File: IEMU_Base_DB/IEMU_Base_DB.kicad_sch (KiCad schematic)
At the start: 0 parts

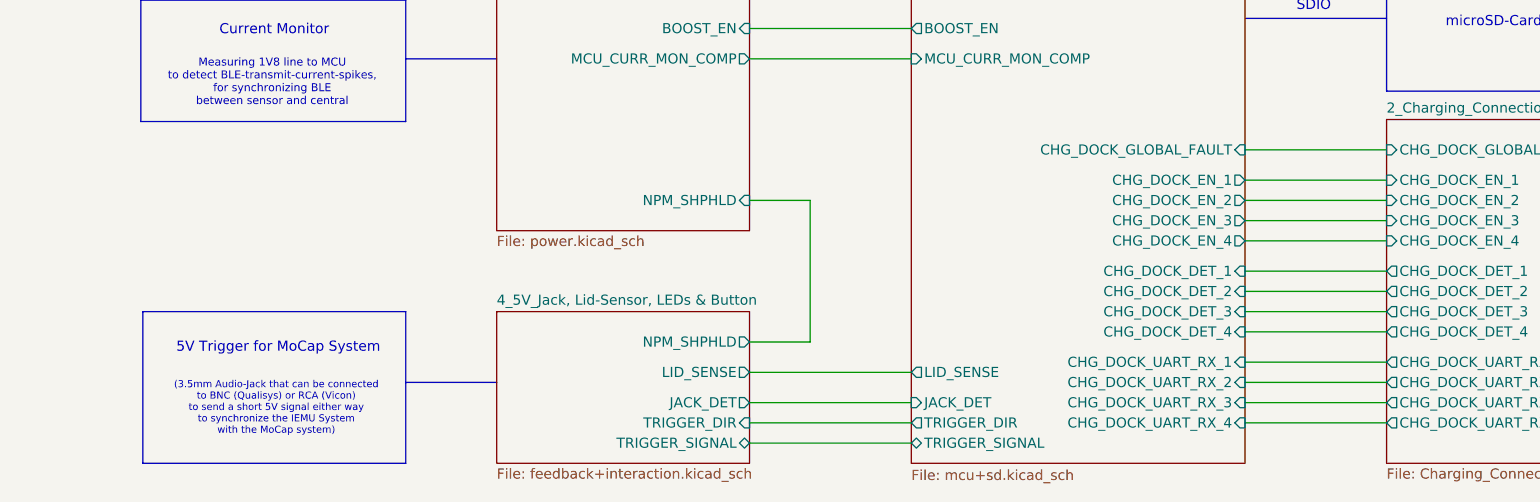
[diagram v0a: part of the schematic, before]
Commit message: implemented changes from the review with TF and fixed lost parts in the library
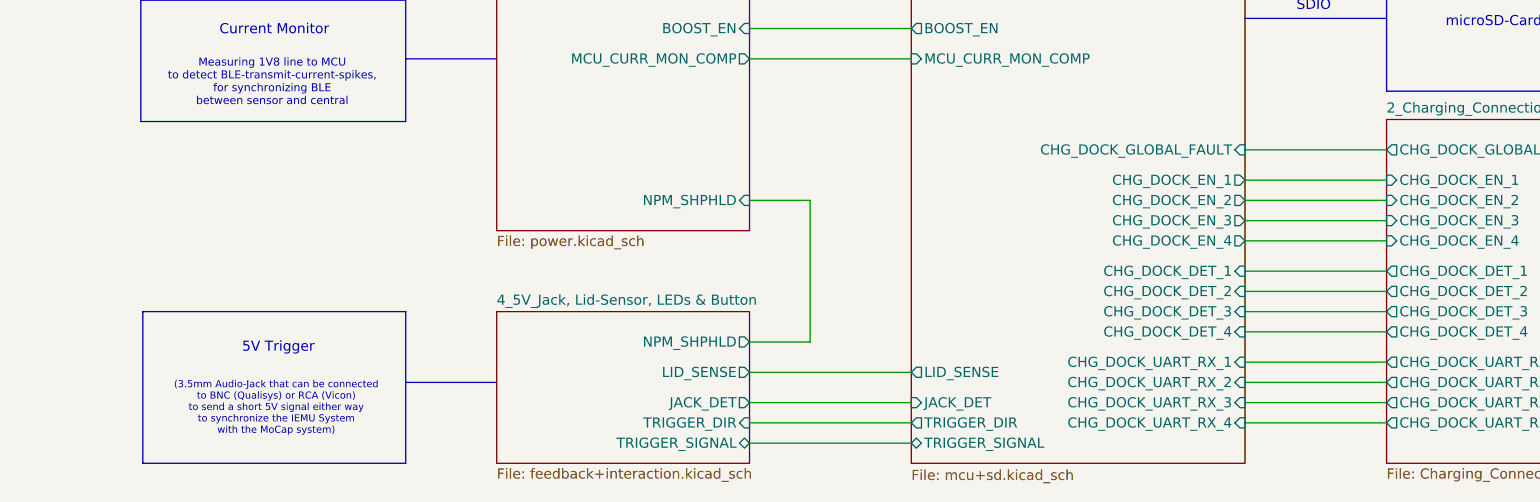
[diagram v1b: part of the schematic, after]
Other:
- note added: "5V Trigger"
- note removed: "5V Trigger for MoCap System"
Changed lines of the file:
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@@
 		)
 	)
-	(text "5V Trigger for MoCap System"
+	(text "5V Trigger"
 		(exclude_from_sim no)
 		(at 42.418 120.142 0)
@@
 			)
 		)
-		(pin "CHG_DOCK_GLOBAL_FAULT" input
-			(at 181.61 95.25 180)
-			(effects
-				(font
-					(size 1.27 1.27)
-				)
-				(justify left)
-			)
-		)
 		(pin "CHG_DOCK_EN_1" input
 			(at 181.61 99.06 180)
@@
 			(effects
 				(font
+					(size 1.27 1.27)
+				)
+				(justify left)
+			)
+		)
+		(pin "CHG_DOCK_GLOBAL_FAULT" output
+			(at 181.61 95.25 180)
+			(effects
+				(font
